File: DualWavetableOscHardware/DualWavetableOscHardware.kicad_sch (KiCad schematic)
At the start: 8 parts, among them U101 STM32F410CBTx, Y101 16MHz

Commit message: rough schematic
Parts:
- added C107, C108: 10u, Capacitor_THT:CP_Radial_D5.0mm_P2.50mm, symbol Device:C_Polarized_US
- added C108: 10n, Capacitor_SMD:C_0805_2012Metric, symbol Device:C
- added C109, C110: 2u2, Capacitor_SMD:C_0805_2012Metric, symbol Device:C
- added C109, C110: 220n, Capacitor_SMD:C_0805_2012Metric, symbol Device:C
- added C111: 4u7, Capacitor_THT:CP_Radial_D4.0mm_P2.00mm, symbol Device:C_Polarized_US
- added C113, C114, C118, C403: 100n, Capacitor_SMD:C_0805_2012Metric, symbol Device:C
- added C115, C406, C408: 10u, Capacitor_THT:CP_Radial_D4.0mm_P2.00mm, symbol Device:C_Polarized_US
- added C404, C405: 2.2u, Capacitor_SMD:C_0805_2012Metric, symbol Device:C
- added C407: 0.1u, Capacitor_SMD:C_0805_2012Metric, symbol Device:C
- added C409, C410: 2.2n, Capacitor_SMD:C_0805_2012Metric, symbol Device:C
- added D504 (x4): D_Schottky, PCM_Diode_SMD_AKL:D_0603_1608Metric, symbol Device:D_Schottky
- added FB101: 90R, Inductor_SMD:L_0805_2012Metric, symbol Device:FerriteBead
- added J102: ~, Connector_PinHeader_2.54mm:ST_SWHeader_3Wire_Pin, symbol Connector:ST_SWDHeader_3Wire
- added J106: MOD2, Connector_Audio:Jack_3.5mm_QingPu_WQP-PJ398SM_Vertical_CircularHoles, symbol Connector_Audio:AudioJack2_SwitchT
- added J106: OUT2, Connector_Audio:Jack_3.5mm_QingPu_WQP-PJ398SM_Vertical_CircularHoles, symbol Connector_Audio:AudioJack2_SwitchT
- added J106: MOD1, Connector_Audio:Jack_3.5mm_QingPu_WQP-PJ398SM_Vertical_CircularHoles, symbol Connector_Audio:AudioJack2_SwitchT
- added J106: CV2, Connector_Audio:Jack_3.5mm_QingPu_WQP-PJ398SM_Vertical_CircularHoles, symbol Connector_Audio:AudioJack2_SwitchT
- added J106: OUT1, Connector_Audio:Jack_3.5mm_QingPu_WQP-PJ398SM_Vertical_CircularHoles, symbol Connector_Audio:AudioJack2_SwitchT
- added J106: CV1, Connector_Audio:Jack_3.5mm_QingPu_WQP-PJ398SM_Vertical_CircularHoles, symbol Connector_Audio:AudioJack2_SwitchT
- added J109: POWER, Connector_PinHeader_2.54mm:PinHeader_2x05_P2.54mm_Vertical, symbol Connector_Generic:Conn_02x05_Odd_Even
- added R137 (x4), R408 (x2): 100k, PCM_Resistor_SMD_AKL:R_0805_2012Metric, symbol Device:R_US
- added R137 (x4): 33k, PCM_Resistor_SMD_AKL:R_0805_2012Metric, symbol Device:R_US
- added R137, R222 (x2), R223 (x4), R408: 10k, PCM_Resistor_SMD_AKL:R_0805_2012Metric, symbol Device:R_US
- added R137: 47k, PCM_Resistor_SMD_AKL:R_0805_2012Metric, symbol Device:R_US
- added R402, R403, R408, R409: 470, PCM_Resistor_SMD_AKL:R_0805_2012Metric, symbol Device:R_US
- added R408 (x2): R_PULLUP, PCM_Resistor_SMD_AKL:R_0805_2012Metric, symbol Device:R_US
- added R408 (x2): 68k, PCM_Resistor_SMD_AKL:R_0805_2012Metric, symbol Device:R_US
- added SW101: RST, Button_Switch_SMD:SW_SPST_B3U-1000P, symbol Switch:SW_SPST
- added SW101: BOOT, Button_Switch_SMD:SW_SPST_B3U-1000P, symbol Switch:SW_SPST
- added SW219: TOGGLE, Button_Switch_THT:SW_PUSH_6mm, symbol Switch:SW_SPST
- added SW221: ENC1, Alps_Rotary_Encoder:RotaryEncoder_Alps_EC11E-Switch_Vertical_H20mm_5Pin, symbol Device:RotaryEncoder_Switch
- added SW221: ENC2, Alps_Rotary_Encoder:RotaryEncoder_Alps_EC11E-Switch_Vertical_H20mm_5Pin, symbol Device:RotaryEncoder_Switch
- added U105: ~, Display:SSD1306_OLED_128x64, symbol Display_Graphic:SSD1306_OLED_128x64
- added U106: AMS1117, Package_TO_SOT_SMD:SOT-223-3_TabPin2, symbol Regulator_Linear:AMS1117
- added U402: TL072, Package_SO:SOIC-8_3.9x4.9mm_P1.27mm, symbol Amplifier_Operational:TL072
- added U403: PCM5100A, Package_SO:TSSOP-20_4.4x6.5mm_P0.65mm, symbol Audio:PCM5100A
- C101, C102, C103, C104, C105, C106: footprint (none) -> Capacitor_SMD:C_0805_2012Metric
- Y101: footprint (none) -> Crystal:Crystal_SMD_EuroQuartz_MT-4Pin_3.2x2.5mm
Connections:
- net +3.3V: now also U101.47 (PDR_ON), C110.1, C114.2, C115.1, FB101.1, R137.1, R222.1, R222.1, R223.1, R223.1, R223.1, R223.1, R408.2, R408.2, R408.2, SW101.1 (A), U105.2 (VCC), U106.2 (VO)
- net CV1_ADC: now also R137.2, R137.2
- net CV2_ADC: now also R137.2, R137.2
- net ENC1_B: now also R223.2, SW221.S1
- net ENC2_B: now also R223.2, SW221.S1
- net ENC2_L: now also R223.2, SW221.A
- net ENC2_R: now also R222.2, SW221.B
- net GND: now also C107.2, C108.1, C108.2, C109.1, C109.2, C110.2, C110.2, C111.2, C113.1, C114.1, C115.2, C118.1, C403.2, C404.2, C406.2, C407.2, C408.2, C409.2, C410.2, J102.1 (GND), J106.S, J106.S, J106.S, J106.S, J106.S, J106.S, J109.3 (Pin_3), J109.4 (Pin_4), J109.5 (Pin_5), J109.6 (Pin_6), J109.7 (Pin_7), J109.8 (Pin_8), R137.1, R137.1, R137.1, R137.1, R137.2, R408.1, R408.1, SW101.2 (B), SW219.2 (B), SW221.C, SW221.C, SW221.S2, SW221.S2, U105.1 (GND), U106.1 (ADJ), U403.10 (DEMP), U403.11 (FLT), U403.16 (FMT), U403.19 (DGND), U403.3 (CPGND), U403.9 (AGND)
- net I2S_BCK: now also U403.13 (BCK)
- net I2S_DIO: now also U403.14 (DIN)
- net I2S_SCK: now also U403.12 (SCK)
- net I2S_WS: now also U403.15 (LRCK)
- net MOD1_ADC: now also R137.2, R137.2
- net MOD2_ADC: now also R137.2, R137.2
- net SCL: now also R408.1, U105.3 (SCL)
- net SDA: now also R408.1, U105.4 (SDA)
- net SWCLK: now also J102.3 (SWCLK)
- net SWDIO: now also J102.4 (SWDIO)
- net TOGGLE_SW: now also R408.1, SW219.1 (A)
- net at U101.22 (VCAP1): now also C111.1
- net BOOT0: now reaches U101.44 (BOOT0)
- net BOOT0: now also R137.1, SW101.2 (B)
- net NRST: now reaches U101.7 (NRST)
- net NRST: now also C118.2, J102.5 (SWO), J102.6 (RST), R137.2, SW101.1 (A)
- net +3.3VA: now reaches U101.9 (VDDA)
- net +3.3VA: now also C108.1, C109.1, C403.1, C406.1, FB101.2, U403.1 (CPVDD), U403.17 (XSMT), U403.20 (DVDD), U403.8 (AVDD)
- new net: D504.1 (K), R137.1 (x4)
- new net: C405.1, U403.2 (CAPP)
- new net: C405.2, U403.4 (CAPM)
- new net: C410.1, R403.2, U402.3 (+)
- new net: C407.1, C408.1, U403.18 (LDOO)
- new net: C409.1, R402.2, U402.5 (+)
- new net: R408.1, R408.2, U402.6 (-)
- new net: R408.1, R408.2, U402.7
- new net: C404.1, U403.5 (VNEG)
- new net: R403.1, U403.7 (OUTR)
- new net: R408.1, R408.2, U402.2 (-)
- new net: R402.1, U403.6 (OUTL)
- new net: R408.2, R409.1, U402.1
- new net +12V: C107.1, C109.2, C113.2, J102.2 (VCC), J109.1 (Pin_1), J109.2 (Pin_2), U106.3 (VI), U402.8 (V+)
- new net -12V: C108.2, C110.1, J109.10 (Pin_10), J109.9 (Pin_9), U402.4 (V-)
- new net CV1: D504.2 (A), J106.T
- new net CV2: D504.2 (A), J106.T
- new net ENC1_L: R223.2, SW221.A
- new net ENC1_R: R222.2, SW221.B
- new net MOD1: D504.2 (A), J106.T
- new net MOD2: D504.2 (A), J106.T
- new net Out1: J106.T, R408.2
- new net Out2: J106.T, R409.2
- no-connect marks 9 -> 15
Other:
- note added: "The DAC gives us 2.1vRMS output which is about 5.9v pk-pk. To get to a standard eurorack amplutude of 10v pk-pk, our output amplifiers need a gain of ~1.7"
- note added: "We'll assume that our CV signals will be 0-10 VDC, so we need to scale inputs by 0.33"
- moved on the sheet: C101, C102, Y101

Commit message: pcb rev 1
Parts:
- added J109: Micro_SD_Card, Connector_Card:microSD_Genesis_Vertical_THT, symbol Connector:Micro_SD_Card
- added R408 (x2): 10k, PCM_Resistor_SMD_AKL:R_0805_2012Metric, symbol Device:R_US
- added SW219: MODE, Button_Switch_THT:SW_PUSH_6mm, symbol Switch:SW_SPST
- C407: value 0.1u -> 100n
- J103: renamed from J102; value ~ -> SWD Header
- SW219: value TOGGLE -> CH
- renumbered C101 to C103, C106 to C104, C105 to C107, C104 to C108, C103 to C112, C108 to C114, C109 to C116, C110 to C118, U105 to U103
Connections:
- net +3.3V: now also J109.4 (VDD), R408.2, R408.2
- net CV1_ADC: now also U101.13 (PA3); no longer U101.10 (PA0)
- net CV2_ADC: now also U101.10 (PA0); no longer U101.12 (PA2)
- net ENC1_L: now also U101.30 (PA9)
- net ENC1_R: now also U101.31 (PA10)
- net ENC2_L: no longer U101.30 (PA9)
- net ENC2_R: no longer U101.31 (PA10)
- net GND: now also J109.6 (VSS), J109.9 (SHIELD), SW219.2 (B)
- net MISO: now also J109.7 (DAT0)
- net MOD1_ADC: now also U101.12 (PA2); no longer U101.11 (PA1)
- net MOD2_ADC: now also U101.11 (PA1); no longer U101.13 (PA3)
- net MOSI: now also J109.3 (CMD)
- net NRST: no longer J103.5 (SWO)
- net SCK: now also J109.5 (CLK)
- net SD_CS: now also J109.2 (DAT3/CD), R408.1
- net SWO: now also J103.5 (SWO)
- net MODE_BTN: now reaches U101.45 (PB8)
- net MODE_BTN: now also R408.1, SW219.1 (A)
- net at R403.1: now also U403.6 (OUTL); no longer U403.7 (OUTR)
- net at R402.1: now also U403.7 (OUTR); no longer U403.6 (OUTL)
- net TOGGLE_SW renamed CH_BTN
- no-connect marks 15 -> 16
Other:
- note added: "Audio DAC and output stage"
- note added: "CV and audio output jacks"
- note added: "Controls and OLED display"
- note added: "MCU and crystal oscillator"
- note added: "MicroSD card reader"
- note added: "Power Connector and 3.3v LDO"
- moved on the sheet: C118, D504, J103, J106, R137, R222, R223, R408, SW101, SW219, SW221, U103

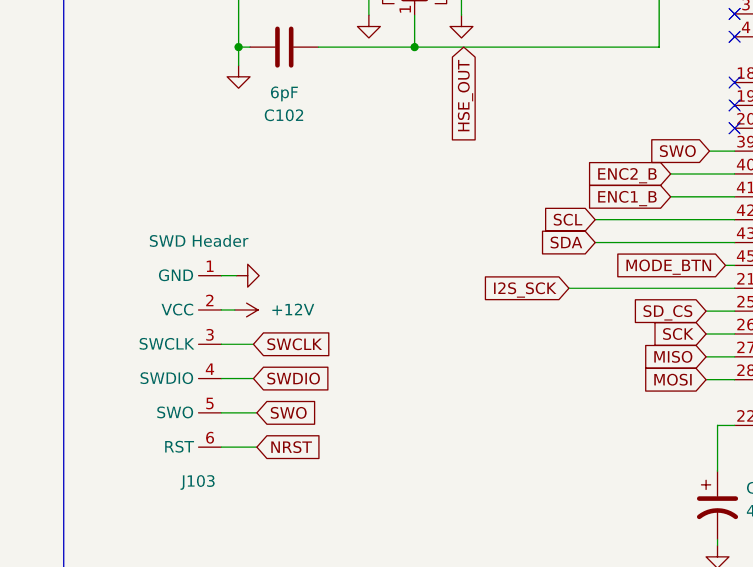
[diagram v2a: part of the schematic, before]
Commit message: double buffer for I2S
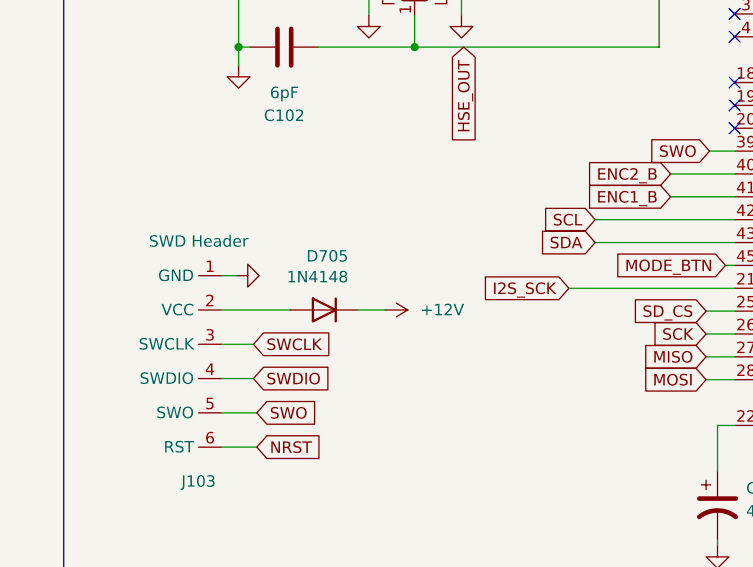
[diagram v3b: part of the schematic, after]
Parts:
- added D705: 1N4148, Diode_SMD:D_SOD-123, symbol Diode:1N4148
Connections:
- net +12V: now also D705.1 (K); no longer J103.2 (VCC)
- new net: D705.2 (A), J103.2 (VCC)
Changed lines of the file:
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@@
+    (stroke (width 0) (type default))
+  )
+  (wire (pts (xy 53.467 116.205) (xy 56.388 116.205))
     (stroke (width 0) (type default))
   )
@@
     (stroke (width 0) (type default))
   )
-  (wire (pts (xy 38.227 116.205) (xy 39.751 116.205))
+  (wire (pts (xy 38.227 116.205) (xy 45.847 116.205))
     (stroke (width 0) (type default))
   )
@@
         (path "/d6d89cf6-c095-4516-adcc-f8fbf926e81c"
           (reference "R315") (unit 1)
+        )
+      )
+    )
+  )
+  (symbol (lib_id "Diode:1N4148") (at 49.657 116.205 0) (mirror y) (unit 1)
+    (in_bom yes) (on_board yes) (dnp no)
+    (property "Reference" "D705" (at 52.324 110.236 0)
+      (effects (font (size 1.27 1.27)) (justify left))
+    )
+    (property "Value" "1N4148" (at 52.324 112.5474 0)
+      (effects (font (size 1.27 1.27)) (justify left))
+    )
+    (property "Footprint" "Diode_SMD:D_SOD-123" (at 49.657 116.205 0)
+      (effects (font (size 1.27 1.27)) hide)
+    )
+    (property "Datasheet" "https://assets.nexperia.com/documents/data-sheet/1N4148_1N4448.pdf" (at 49.657 116.205 0)
+      (effects (font (size 1.27 1.27)) hide)
+    )
+    (property "Sim.Device" "D" (at 49.657 116.205 0)
+      (effects (font (size 1.27 1.27)) hide)
+    )
+    (property "Sim.Pins" "1=K 2=A" (at 49.657 116.205 0)
+      (effects (font (size 1.27 1.27)) hide)
+    )
+    (pin "1")
+    (pin "2")
+    (instances
+      (project "ESP808_mk3"
+        (path "/1b0f4827-7224-4696-9105-e83073878432/6d702576-90e6-405d-b6f2-7489acbb0af2/8daf6f73-7e21-4c83-8271-23ce5b907f74"
+          (reference "D705") (unit 1)
+        )
+      )
+      (project "ESP808"
+        (path "/36804e49-266f-4323-9d1a-a2cb3256aa72/00000000-0000-0000-0000-000064d2a871"
+          (reference "D205") (unit 1)
+        )
+      )
+      (project "Kicks"
+        (path "/4a47122c-e783-4338-8c58-f4151402667e"
+          (reference "D205") (unit 1)
+        )
+      )
+      (project "DualWavetableOscHardware"
+        (path "/86aa4a86-4a4a-487e-b6f4-ec263cd9c3f4"
+          (reference "D105") (unit 1)
+        )
+      )
+      (project "Kicks"
+        (path "/e35b18c2-7599-4b98-abb1-7c0c35e05a64"
+          (reference "D705") (unit 1)
         )
       )
@@
     )
   )
-  (symbol (lib_id "power:+12V") (at 39.751 116.205 270) (unit 1)
-    (in_bom yes) (on_board yes) (dnp no) (fields_autoplaced)
-    (property "Reference" "#PWR0107" (at 35.941 116.205 0)
-      (effects (font (size 1.27 1.27)) hide)
-    )
-    (property "Value" "+12V" (at 43.688 116.205 90)
-      (effects (font (size 1.27 1.27)) (justify left))
-    )
-    (property "Footprint" "" (at 39.751 116.205 0)
-      (effects (font (size 1.27 1.27)) hide)
-    )
-    (property "Datasheet" "" (at 39.751 116.205 0)
-      (effects (font (size 1.27 1.27)) hide)
-    )
+  (symbol (lib_id "power:+12V") (at 56.388 116.205 270) (unit 1)
+    (in_bom yes) (on_board yes) (dnp no) (fields_autoplaced)
+    (property "Reference" "#PWR0107" (at 52.578 116.205 0)
+      (effects (font (size 1.27 1.27)) hide)
+    )
+    (property "Value" "+12V" (at 60.325 116.205 90)
+      (effects (font (size 1.27 1.27)) (justify left))
+    )
+    (property "Footprint" "" (at 56.388 116.205 0)
+      (effects (font (size 1.27 1.27)) hide)
+    )
+    (property "Datasheet" "" (at 56.388 116.205 0)
+      (effects (font (size 1.27 1.27)) hide)
+    )

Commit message: status LEDs and test points
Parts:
- added D106: LED_GRN, LED_THT:LED_D3.0mm, symbol Device:LED
- added D107: LED_RED, LED_THT:LED_D3.0mm, symbol Device:LED
- added R408 (x2): 220, PCM_Resistor_SMD_AKL:R_0805_2012Metric, symbol Device:R_US
- added TP101: I2S_SCK, TestPoint:TestPoint_Pad_D1.0mm_Value, symbol Connector:TestPoint
- added TP102: I2S_BCK, TestPoint:TestPoint_Pad_D1.0mm_Value, symbol Connector:TestPoint
- added TP103: 3V3A, TestPoint:TestPoint_Pad_D1.0mm_Value, symbol Connector:TestPoint
- added TP104: 3V3, TestPoint:TestPoint_Pad_D1.0mm_Value, symbol Connector:TestPoint
- added TP105: DAC_R, TestPoint:TestPoint_Pad_D1.0mm_Value, symbol Connector:TestPoint
- added TP106: DAC_L, TestPoint:TestPoint_Pad_D1.0mm_Value, symbol Connector:TestPoint
- added TP107: ADC1_0, TestPoint:TestPoint_Pad_D1.0mm_Value, symbol Connector:TestPoint
- added TP108: ADC1_1, TestPoint:TestPoint_Pad_D1.0mm_Value, symbol Connector:TestPoint
- added TP109: I2S_SD, TestPoint:TestPoint_Pad_D1.0mm_Value, symbol Connector:TestPoint
- added TP110: I2S_LR, TestPoint:TestPoint_Pad_D1.0mm_Value, symbol Connector:TestPoint
- added TP111: ADC1_2, TestPoint:TestPoint_Pad_D1.0mm_Value, symbol Connector:TestPoint
- added TP112: ADC1_3, TestPoint:TestPoint_Pad_D1.0mm_Value, symbol Connector:TestPoint
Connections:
- net +3.3V: now also TP104.1
- net +3.3VA: now also TP103.1
- net CV1_ADC: now also TP112.1
- net CV2_ADC: now also TP107.1
- net GND: now also D106.1 (K), D107.1 (K)
- net I2S_BCK: now also TP102.1
- net I2S_DIO: now also TP109.1
- net I2S_SCK: now also TP101.1
- net I2S_WS: now also TP110.1
- net MOD1_ADC: now also TP111.1
- net MOD2_ADC: now also TP108.1
- net LED_GRN: now reaches U101.19 (PB1)
- net LED_GRN: now also R408.2
- net LED_RED: now reaches U101.20 (PB2)
- net LED_RED: now also R408.2
- net at R403.1, U403.6 (OUTL): now also TP106.1
- net at R402.1, U403.7 (OUTR): now also TP105.1
- new net: D106.2 (A), R408.1
- new net: D107.2 (A), R408.1
- no-connect marks 16 -> 14
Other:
- note added: "Datasheet says GPIOs can do up to 25mA but we'll keep it around 15"
- note added: "Status LEDs"
- moved on the sheet: J109, R408

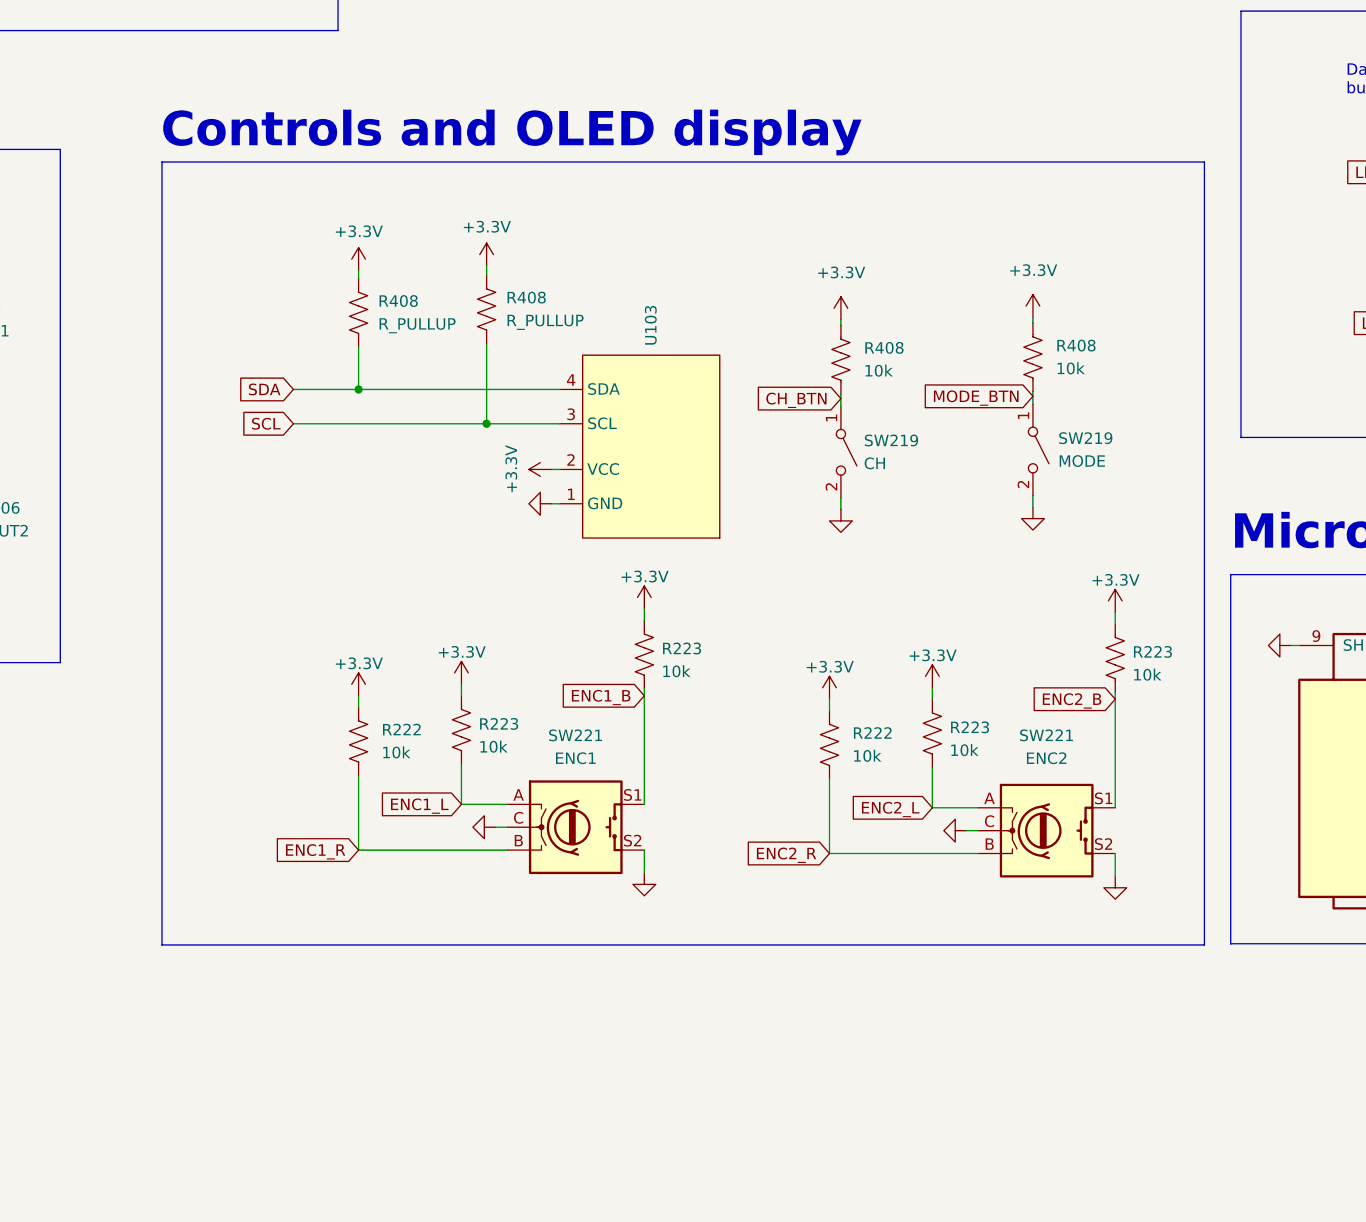
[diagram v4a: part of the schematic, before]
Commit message: status LED code
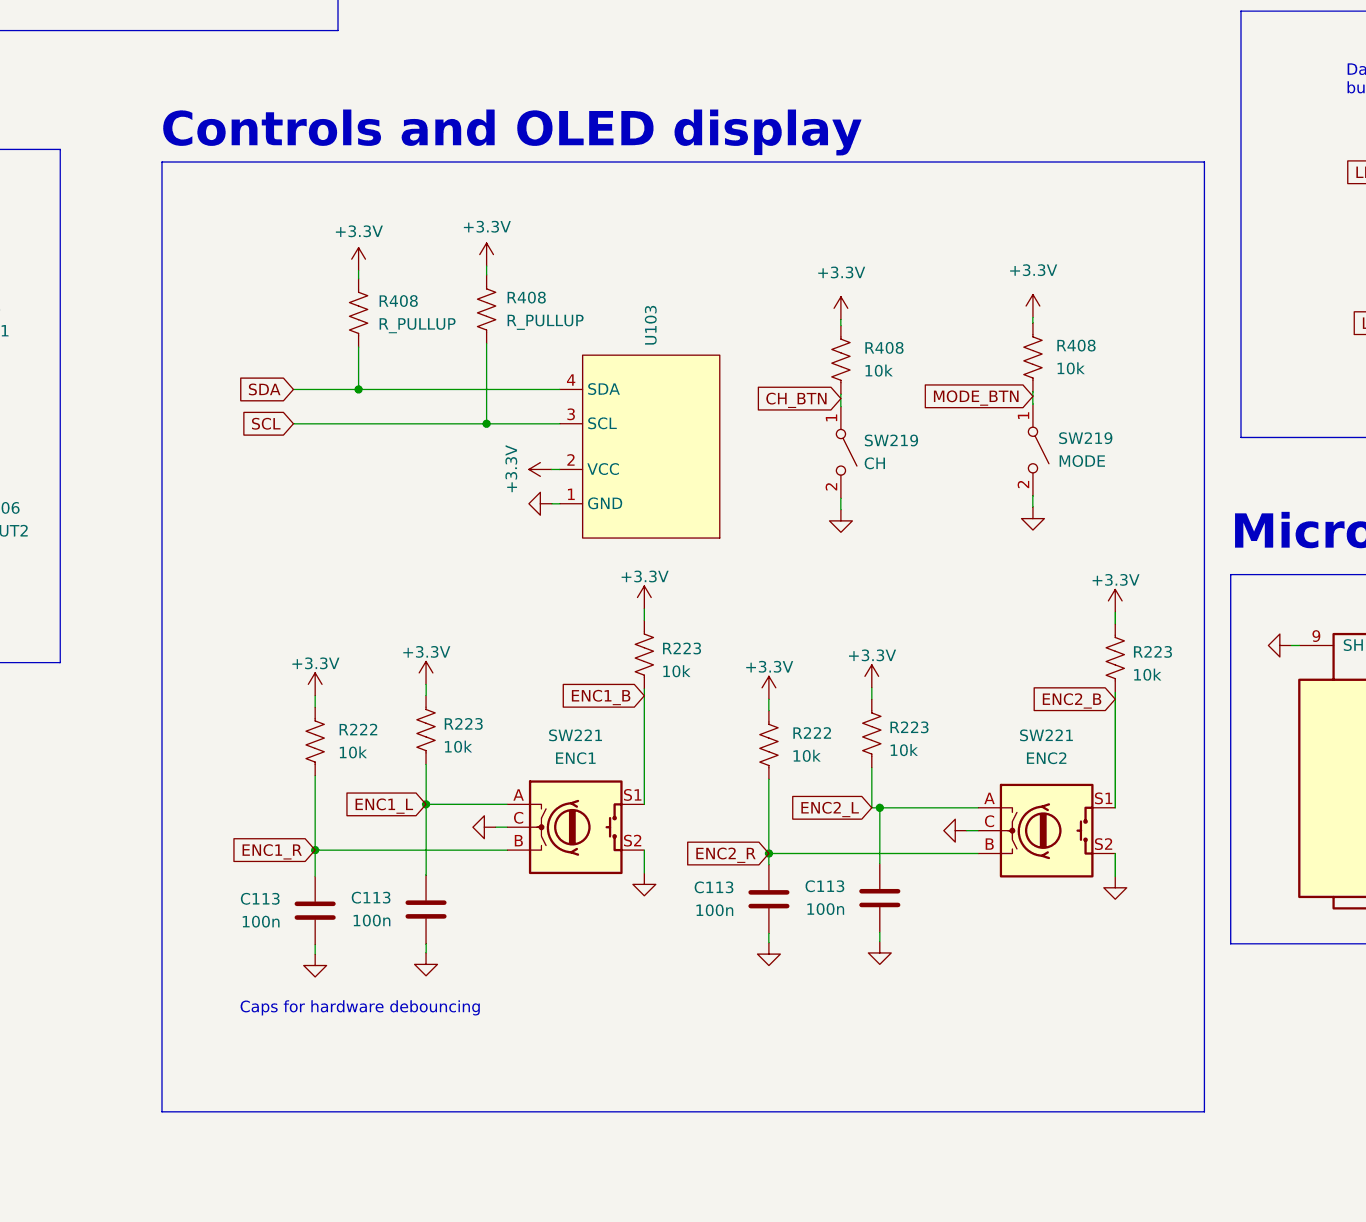
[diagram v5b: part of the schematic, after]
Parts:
- added C113 (x4): 100n, Capacitor_SMD:C_0805_2012Metric, symbol Device:C
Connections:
- net ENC1_L: now also C113.2
- net ENC1_R: now also C113.2
- net ENC2_L: now also C113.2
- net ENC2_R: now also C113.2
- net GND: now also C113.1, C113.1, C113.1, C113.1
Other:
- note added: "Caps for hardware debouncing"
- moved on the sheet: R222, R223
